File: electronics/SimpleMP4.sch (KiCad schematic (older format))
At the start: 141 parts

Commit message: added annotations to components
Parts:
- gave numbers to parts that had none: 141
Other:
- moved on the sheet: C53, C54, C55, C56, C57, C58, D3, L6, R38, R39, R40, R41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

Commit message: added proper display and  LCD backlight driver
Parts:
- removed C53, C55, C56, C57: 105, symbol C
- removed C54: 104, symbol C
- removed D3: 1N5819, symbol D
- removed J2: DISPLAY, symbol CONN_01X36
- removed L6: 10uH, symbol L
- removed R38: 0R, symbol R
- removed R39: 47K, symbol R
- removed R44: 12R, symbol R
- removed U10: CR1937, symbol CR1937
- added C? (x2): 104, symbol C
- added J?: DISPLAY, symbol CONN_01X37
- added U?: ZLED7012, symbol ZLED7012
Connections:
- net labels added: LEDK1, LEDK2, LEDK3, LEDK4, VB, VLED, XL, XR, YD, YU
- net labels removed: LED+, LED-1
- wire segments 493 -> 488
- no-connect marks 33 -> 37

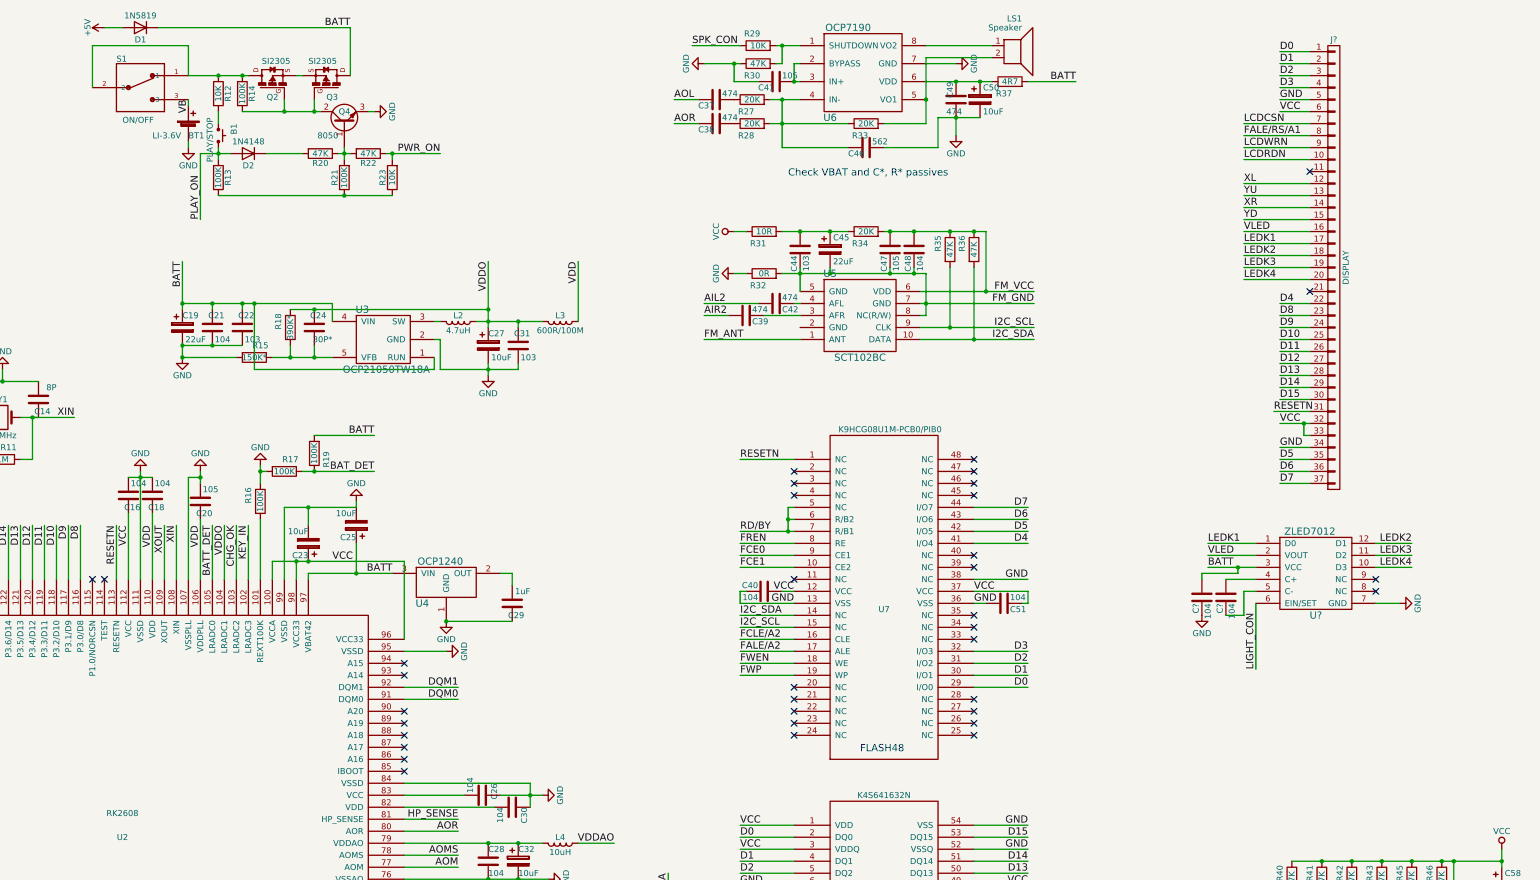
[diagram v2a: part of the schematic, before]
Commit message: added TRS 5pin audio jack section
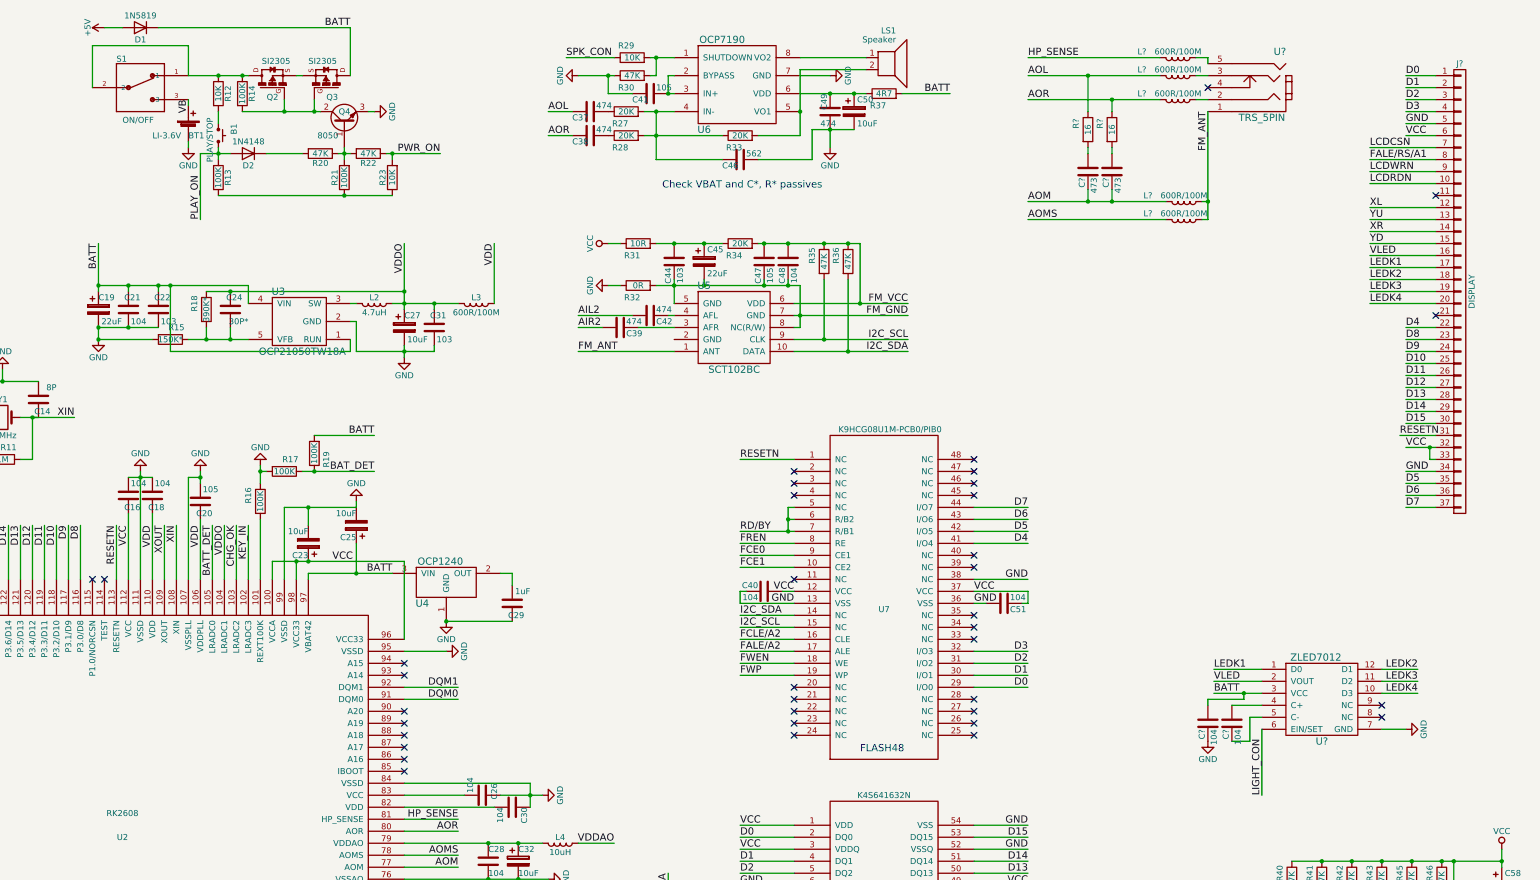
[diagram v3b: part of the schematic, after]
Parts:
- added C? (x2): 473, symbol C
- added L? (x5): 600R/100M, symbol L
- added R? (x2): 16, symbol R
- added U?: TRS_5PIN, symbol TRS_5PIN
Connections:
- net AOL: now also L?.2, R?.1
- net AOM: now also C?.1, C?.1, L?.2
- net AOMS: now also L?.2
- net AOR: now also L?.2, R?.1
- net FM_ANT: now also L?.1, L?.1, U?.1
- net HP_SENSE: now also L?.2
- new net: L?.1, U?.2
- new net: L?.1, U?.3
- new net: L?.1, U?.5
- new net: C?.2, R?.2 (x2)
- no-connect marks 37 -> 38
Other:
- moved on the sheet: C19, C21, C22, C24, C27, C31, C37, C38, C39, C41, C42, C44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

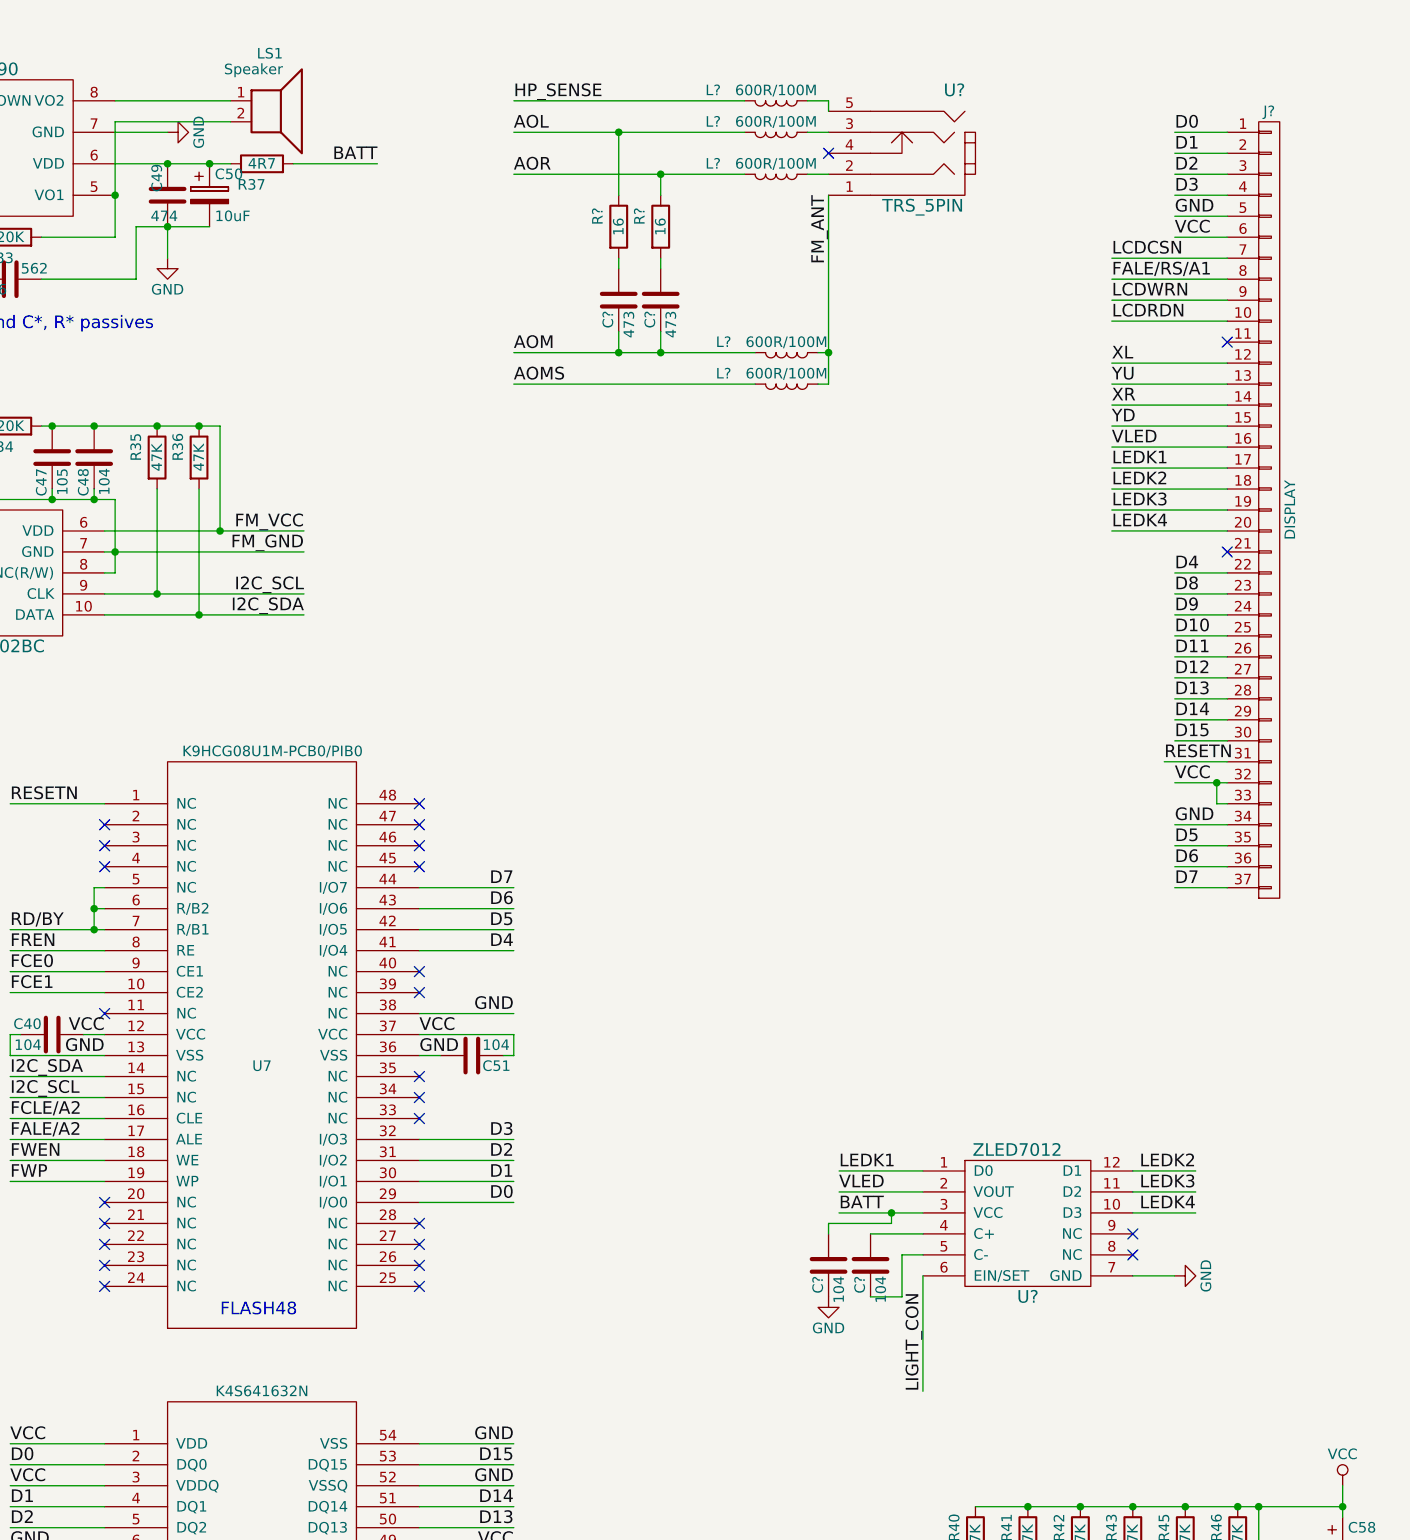
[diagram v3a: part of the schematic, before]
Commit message: added NOR Flash chip
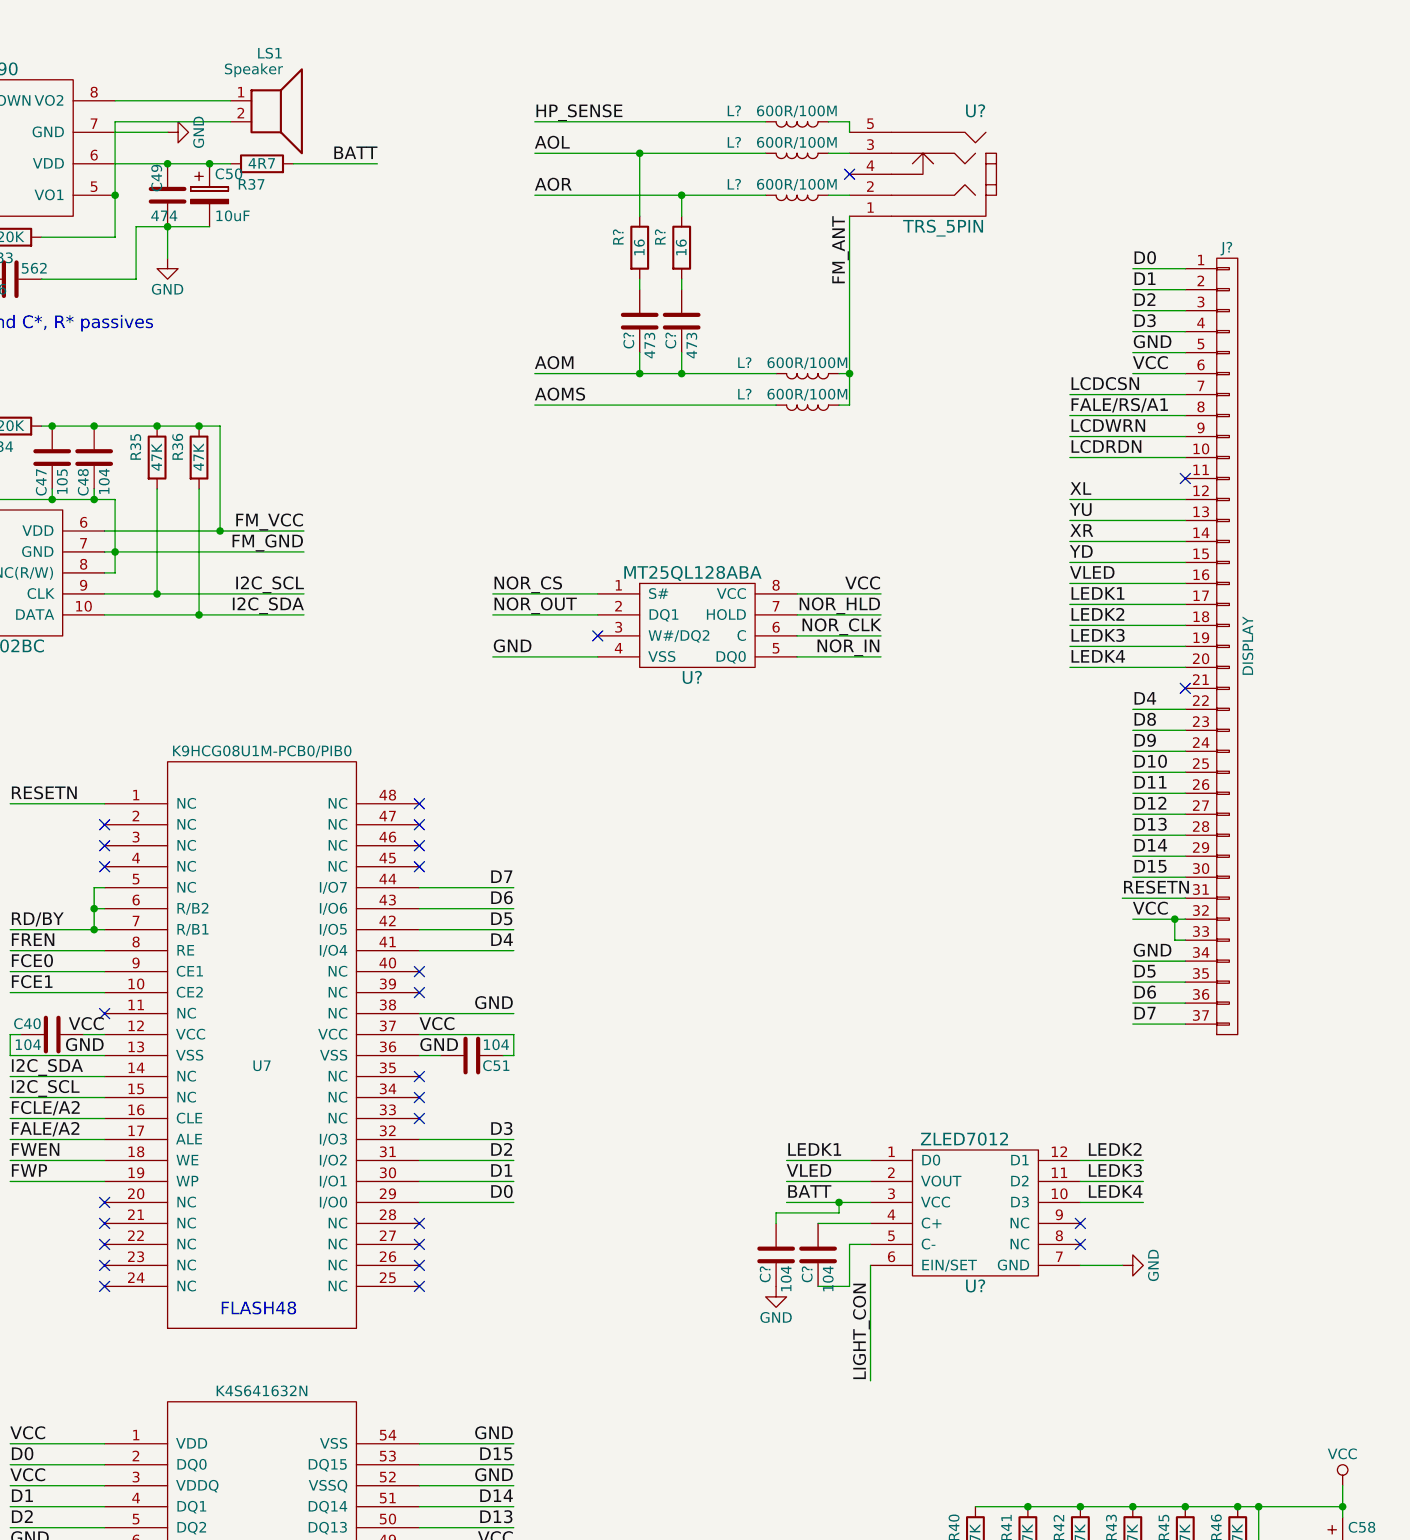
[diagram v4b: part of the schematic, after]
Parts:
- added U?: MT25QL128ABA, symbol MT25QL128ABA
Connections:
- net GND: now also U?.4 (VSS)
- net VCC: now also U?.8 (VCC)
- new net NOR_CLK: U?.6 (C)
- new net NOR_CS: U?.1 (S#)
- new net NOR_HLD: U?.7 (HOLD)
- new net NOR_IN: U?.5 (DQ0)
- new net NOR_OUT: U?.2 (DQ1)
- no-connect marks 38 -> 39
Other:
- moved on the sheet: C?, J?, L?, R?, U?

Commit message: added annotations and bom
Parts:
- removed C37, C38, C39, C42, C49: 474, symbol C
- removed C41, C47: 105, symbol C
- removed C44: 103, symbol C
- removed C45: 22uF, symbol CP
- removed C46: 562, symbol C
- removed C48: 104, symbol C
- removed C50: 10uF, symbol CP
- removed LS1: Speaker, symbol Speaker
- removed R27, R28, R33, R34: 20K, symbol R
- removed R29: 10K, symbol R
- removed R30, R35, R36: 47K, symbol R
- removed R31: 10R, symbol R
- removed R32: 0R, symbol R
- removed R37: 4R7, symbol R
- removed U5: SCT102BC, symbol SCT102BC
- removed U6: OCP7190, symbol OCP7190
- gave numbers to parts that had none: 15
- renumbered C20 to C19, C19 to C20, C25 to C24, C24 to C25, C28 to C27, C29 to C28, C30 to C29, C32 to C30, C27 to C31, C33 to C32, C31 to C33, C40 to C37, C43 to C38, C51 to C41, C52 to C42, C58 to C45, L4 to L3, L3 to L4, R16 to R12, R17 to R13, R15 to R14, R19 to R15, R18 to R16, R12 to R17, R13 to R18, R14 to R19, R24 to R20, R20 to R21, R25 to R22, R21 to R23, R22 to R24, R26 to R25, R23 to R26, R40 to R29, R41 to R30, R42 to R31, R43 to R32, R45 to R33, R46 to R34, U7 to U6, U8 to U7
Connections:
- net VCC: now also C28.2, U4.2 (OUT)
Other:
- note removed: "Check VBAT and C*, R* passives"
- moved on the sheet: B1, BT1, C20, C21, C22, C25, C31, C33, C39, C40, D1, D2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
